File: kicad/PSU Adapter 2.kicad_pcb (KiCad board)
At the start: 2 copper layers, 55 x 80 mm, 18 parts, among them J1 AC Connector, J2 ATX From PSU, J3 Power to Logic Board, J4 Fan, J5 Power to PSU, J6 Conn_01x05_Pin, K1 AC Passthrough Relay, U1 TLP521-1

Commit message: Add files via upload
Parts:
- removed J2: ATX From PSU, Connector_Molex:Molex_Mini-Fit_Jr_5566-20A_2x10_P4.20mm_Vertical
- added J7: ATX-24, Connector_Molex:Molex_Mini-Fit_Jr_5566-24A_2x12_P4.20mm_Vertical, F.Cu at (135.0, 161.0)
- moved REF** 5.00 mm to (140.0, 106.0)
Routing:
- net /+5V: track 68.9 -> 74.0 mm
- net /+12V: track 98.6 -> 102.0 mm

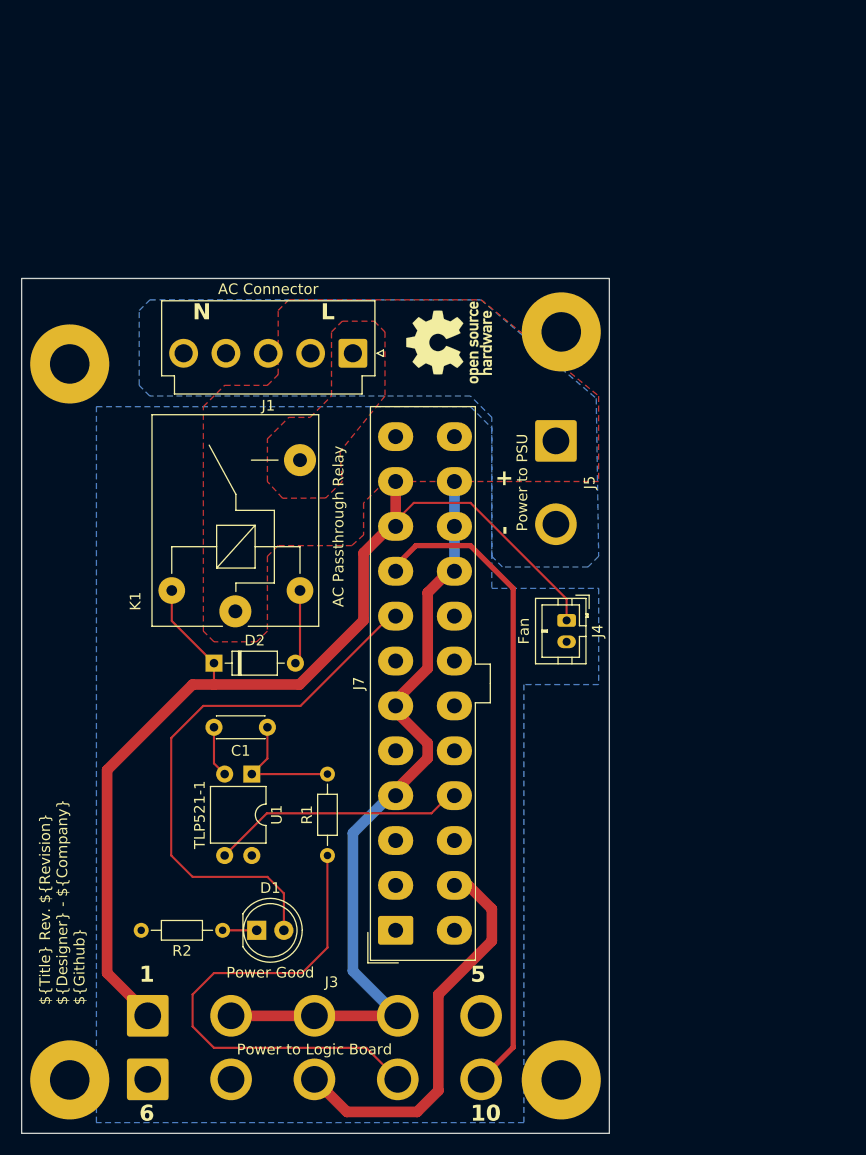
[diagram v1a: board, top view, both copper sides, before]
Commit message: Add files via upload
Updated to rev 0.3 including footprint for Chinese ATX connector which has 4.2mm pitch between rows (Molex spec is 5.5mm)
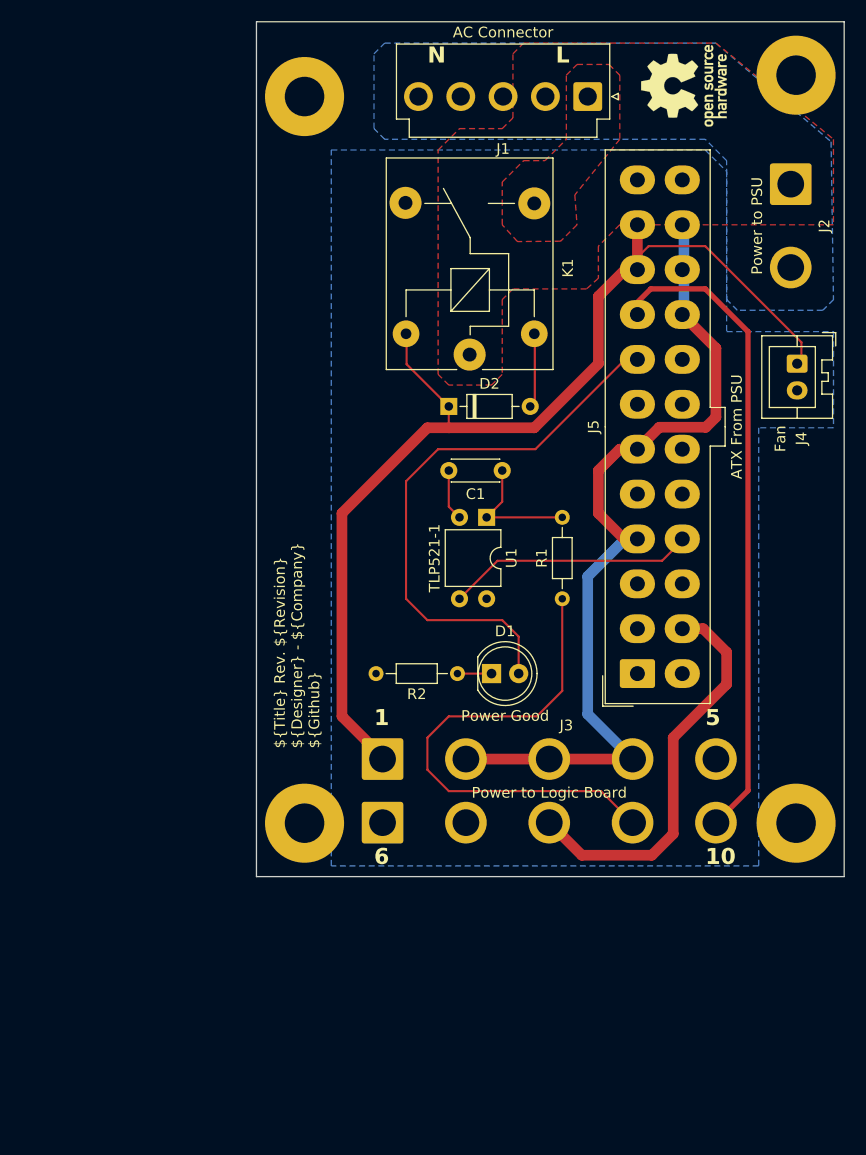
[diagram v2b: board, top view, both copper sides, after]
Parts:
- J4: footprint Connector_JST:JST_PH_B2B-PH-K_1x02_P2.00mm_Vertical -> Connector_JST:JST_XA_B02B-XASK-1_1x02_P2.50mm_Vertical
- J5: renamed from J7; value ATX-24 -> ATX From PSU; footprint Connector_Molex:Molex_Mini-Fit_Jr_5566-24A_2x12_P4.20mm_Vertical -> Library:Molex_Mini-Fit_Jr_5566-24A_2x12_P4.20mm_Vertical_Chinese
- K1: footprint Relay_THT:Relay_SPST_SANYOU_SRD_Series_Form_A -> Relay_THT:Relay_SPDT_SANYOU_SRD_Series_Form_C
- moved H1 33.3 mm to (126.5, 83.0)
- moved J3 32.6 mm to (133.8, 145.0)
- moved C1 32.6 mm to (145.0, 118.0)
- moved D1 32.6 mm to (144.0, 137.0)
- moved D2 32.6 mm to (140.0, 112.0)
- moved H2 32.6 mm to (172.5, 81.0)
- moved H3 32.6 mm to (126.5, 151.0)
- moved H4 32.6 mm to (172.5, 151.0)
- moved J1 32.6 mm to (153.0, 83.0)
- moved J2 32.6 mm to (172.0, 91.2)
- moved J5 32.6 mm to (157.0, 137.0)
- moved R1 32.6 mm to (150.6, 130.0)
- moved R2 32.6 mm to (140.8, 137.0)
- moved REF** 32.6 mm to (162.0, 82.0)
- moved J6 32.6 mm to (133.8, 150.9)
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- renumbered J5 to J2
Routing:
- net /+5V: track 74.0 -> 80.7 mm
- net /PWR_OK: track 51.7 -> 52.8 mm
- net /+12V: track 102.0 -> 102.5 mm
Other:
- board text added: "+12V"
- board text added: "+5V"
- board text added: "+5VSB"
- board text added: "-12V"
- board text added: "GND"
- board text added: "PFW"
- board text removed: "- +"
